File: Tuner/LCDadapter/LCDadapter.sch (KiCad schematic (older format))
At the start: 30 parts, among them J1 Conn_02x05_Odd_Even, J2 Conn_01x01, J3 Conn_01x01, J4 Conn_01x01, J5 Conn_01x01, Q1 2N3904, SW1 SW_Push, SW2 SW_Push, SW3 SW_Push, SW4 SW_Push, SW5 SW_Push, SW6 SW_Push, U1 PCF8574, U2 LCD-016N002L

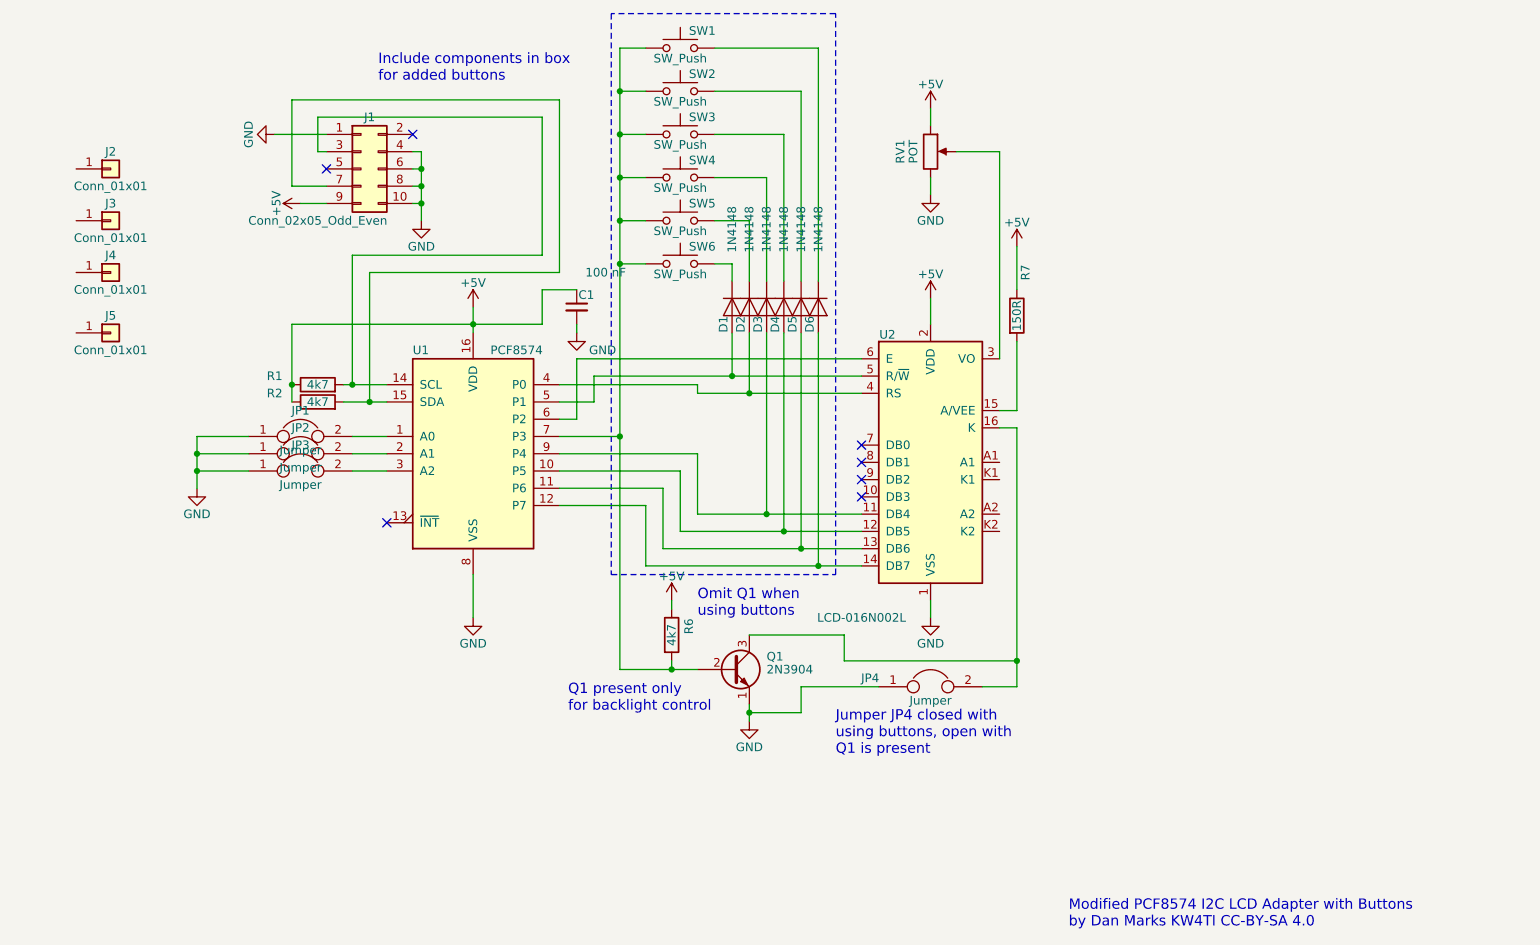
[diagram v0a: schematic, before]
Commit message: Added some initial I2C user interface stuff
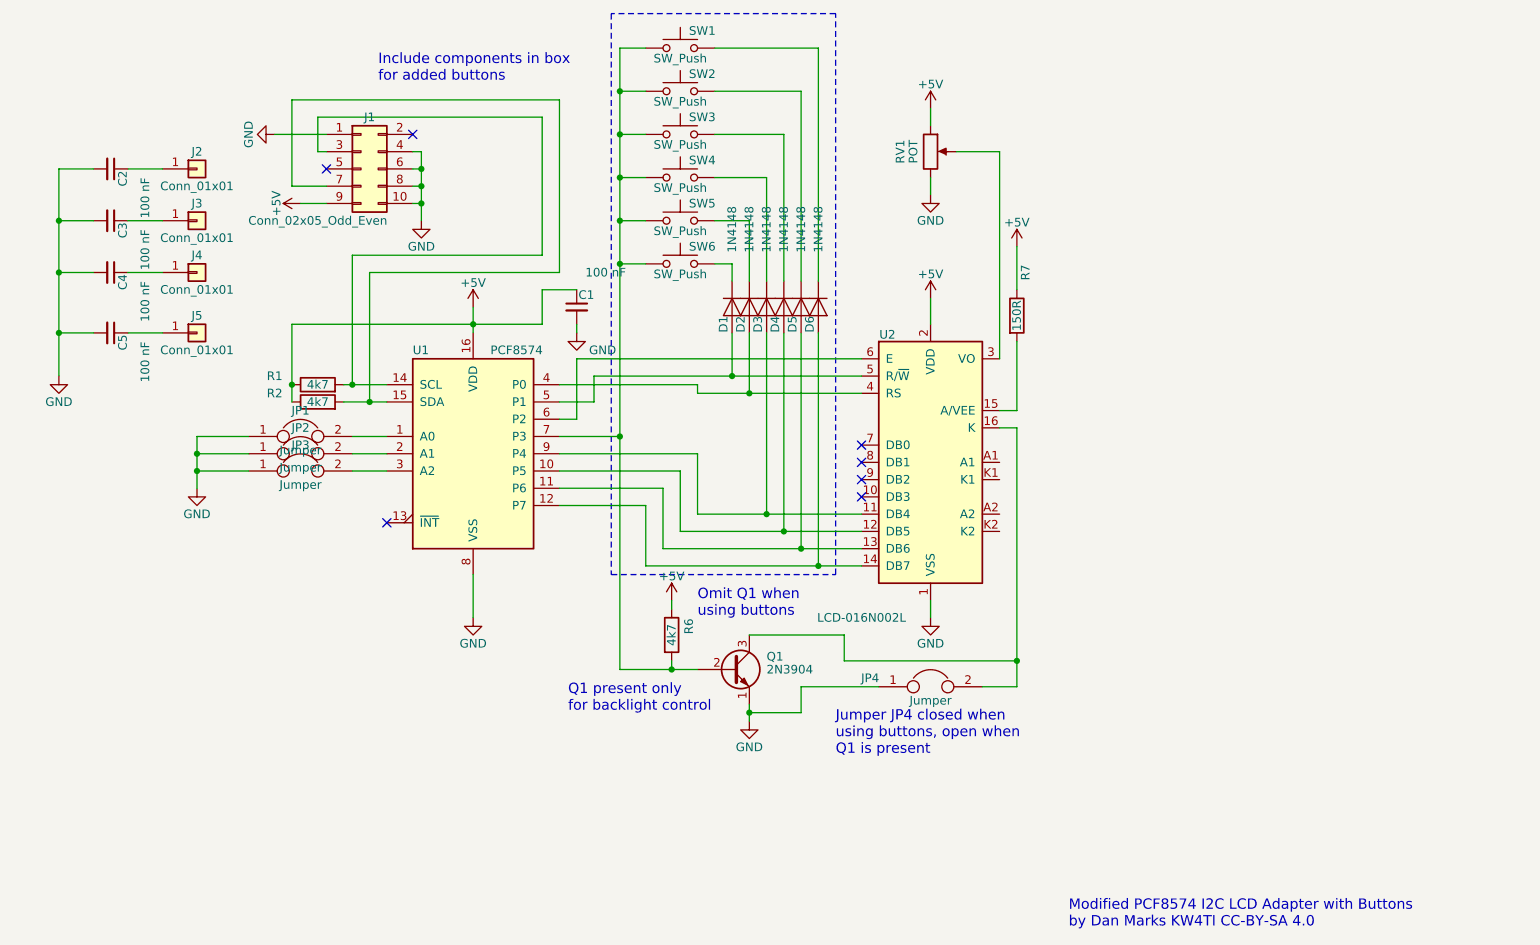
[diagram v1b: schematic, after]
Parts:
- added C2, C3, C4, C5: 100 nF, Capacitors_THT:C_Disc_D5.0mm_W2.5mm_P2.50mm, symbol C_Small
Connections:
- net GND: now also C2.2, C3.2, C4.2, C5.2
- net at J2.1 (Pin_1): now also C2.1
- net at J3.1 (Pin_1): now also C3.1
- net at J4.1 (Pin_1): now also C4.1
- net at J5.1 (Pin_1): now also C5.1
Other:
- note added: "Jumper JP4 closed when\nusing buttons, open when\nQ1 is present\n"
- note removed: "Jumper JP4 closed with\nusing buttons, open with\nQ1 is present\n"
- moved on the sheet: J2, J3, J4, J5

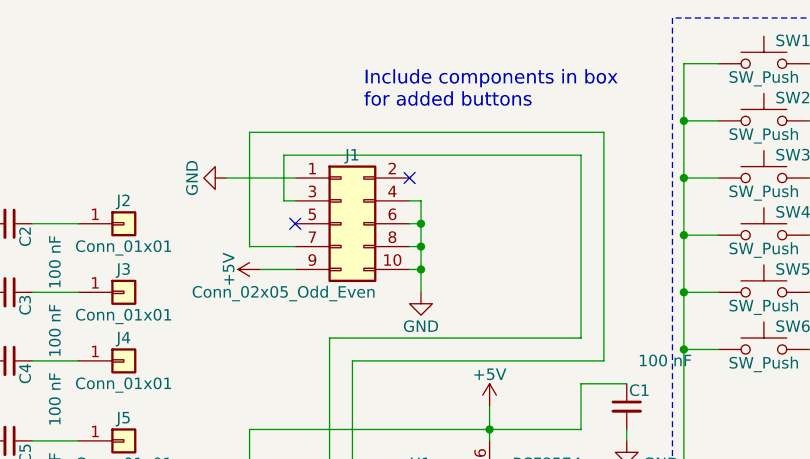
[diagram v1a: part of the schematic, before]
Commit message: Added nonswitched output to ReversibleSections
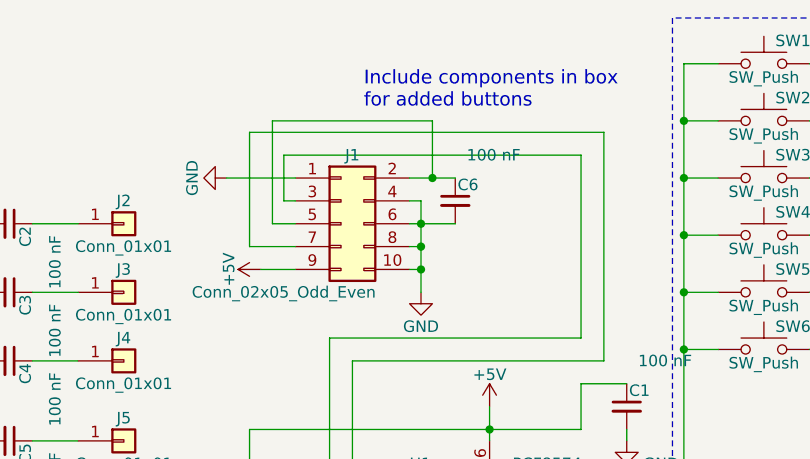
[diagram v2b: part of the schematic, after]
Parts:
- added C6: 100 nF, Capacitors_THT:C_Disc_D5.0mm_W2.5mm_P2.50mm, symbol C_Small
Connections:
- net GND: now also C6.2
- net at J1.2 (Pin_2): now also J1.5 (Pin_5), C6.1
- no-connect marks 7 -> 5
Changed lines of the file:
@@
 	0    -1   -1   0
 $EndComp
-NoConn ~ 3650 2250
-NoConn ~ 3150 2450
 NoConn ~ 3500 4500
 $Comp
@@
 	3700 2350 3650 2350
 Wire Wire Line
-	3700 2450 3650 2450
+	3650 2450 3850 2450
 Connection ~ 3700 2450
 Wire Wire Line
@@
 Wire Wire Line
 	1600 3400 1800 3400
+Wire Wire Line
+	3150 2450 3050 2450
+Wire Wire Line
+	3050 2450 3050 2000
+Wire Wire Line
+	3050 2000 3750 2000
+Wire Wire Line
+	3750 2000 3750 2250
+Wire Wire Line
+	3650 2250 3850 2250
+$Comp
+L C_Small C6
+U 1 1 5C9AA30F
+P 3850 2350
+F 0 "C6" H 3860 2420 50  0000 L CNN
+F 1 "100 nF" H 3900 2550 50  0000 L CNN
+F 2 "Capacitors_THT:C_Disc_D5.0mm_W2.5mm_P2.50mm" H 3850 2350 50  0001 C CNN
+F 3 "" H 3850 2350 50  0001 C CNN
+	1    3850 2350
+	1    0    0    -1
+$EndComp
+Connection ~ 3750 2250
 $EndSCHEMATC

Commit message: LCDAdapter added dual polarity set I2C address
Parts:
- removed JP1, JP2, JP3: Jumper, Pin_Headers:Pin_Header_Straight_1x02_Pitch2.54mm, symbol Jumper
- added JP1, JP2, JP3: Jumper_NC_Dual, Pin_Headers:Pin_Header_Straight_1x03_Pitch2.54mm, symbol Jumper_NC_Dual
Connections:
- net +5V: now also JP1.1, JP2.1, JP3.1
- net GND: now also JP1.3, JP2.3, JP3.3
- net at U1.1 (A0): now also JP1.2
- net at U1.2 (A1): now also JP2.2
- net at U1.3 (A2): now also JP3.2
